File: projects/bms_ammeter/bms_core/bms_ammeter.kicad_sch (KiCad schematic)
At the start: 9 parts, among them IC1 ADS1246IPWR, U2 AP7370-12FDC, U3 ADUM4150ARIZ-RL

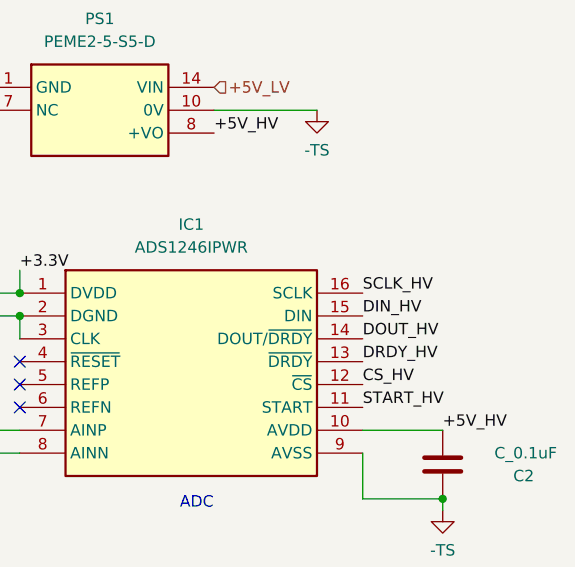
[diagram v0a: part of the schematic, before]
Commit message: Added ammeter to BMS core schematic
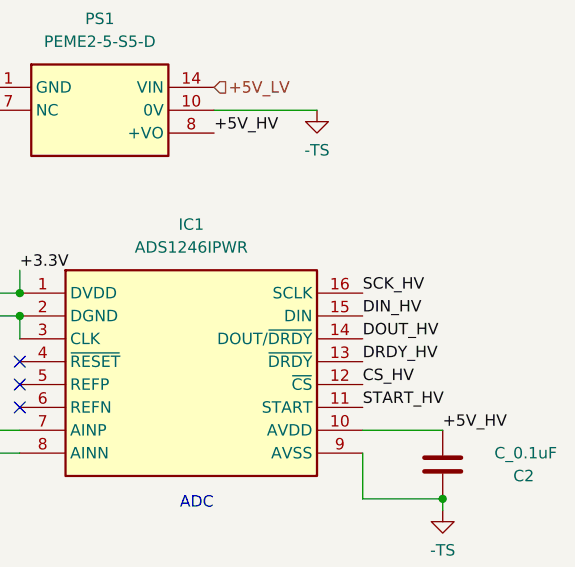
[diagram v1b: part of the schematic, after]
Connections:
- net SCLK_HV is gone; now on net SCK_HV: IC1.16 (SCLK)
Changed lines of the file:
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@@
     (effects (font (size 1.27 1.27)) (justify left bottom))
   )
-  (label "SCLK_HV" (at 191.77 83.82 0) (fields_autoplaced)
+  (label "SCK_HV" (at 191.77 83.82 0) (fields_autoplaced)
     (effects (font (size 1.27 1.27)) (justify left bottom))
   )
@@
     (instances
       (project "bms_core"
-        (path "/19b2a9f9-0be6-4bde-80c5-cbc5126d55d5/fa7f3556-5e5e-451a-bb56-11a595d3a0ce"
+        (path "/19b2a9f9-0be6-4bde-80c5-cbc5126d55d5/ed6af89d-de77-4c92-a6f5-d304e6bc128b"
           (reference "#PWR08") (unit 1)
         )
@@
     (instances
       (project "bms_core"
-        (path "/19b2a9f9-0be6-4bde-80c5-cbc5126d55d5/fa7f3556-5e5e-451a-bb56-11a595d3a0ce"
+        (path "/19b2a9f9-0be6-4bde-80c5-cbc5126d55d5/ed6af89d-de77-4c92-a6f5-d304e6bc128b"
           (reference "#PWR02") (unit 1)
         )
@@
     (instances
       (project "bms_core"
-        (path "/19b2a9f9-0be6-4bde-80c5-cbc5126d55d5/fa7f3556-5e5e-451a-bb56-11a595d3a0ce"
+        (path "/19b2a9f9-0be6-4bde-80c5-cbc5126d55d5/ed6af89d-de77-4c92-a6f5-d304e6bc128b"
           (reference "IC1") (unit 1)
         )
@@
     (instances
       (project "bms_core"
-        (path "/19b2a9f9-0be6-4bde-80c5-cbc5126d55d5/fa7f3556-5e5e-451a-bb56-11a595d3a0ce"
+        (path "/19b2a9f9-0be6-4bde-80c5-cbc5126d55d5/ed6af89d-de77-4c92-a6f5-d304e6bc128b"
           (reference "#PWR01") (unit 1)
         )
@@
     (instances
       (project "bms_core"
-        (path "/19b2a9f9-0be6-4bde-80c5-cbc5126d55d5/fa7f3556-5e5e-451a-bb56-11a595d3a0ce"
+        (path "/19b2a9f9-0be6-4bde-80c5-cbc5126d55d5/ed6af89d-de77-4c92-a6f5-d304e6bc128b"
           (reference "#PWR010") (unit 1)
         )
@@
     (instances
       (project "bms_core"
-        (path "/19b2a9f9-0be6-4bde-80c5-cbc5126d55d5/fa7f3556-5e5e-451a-bb56-11a595d3a0ce"
+        (path "/19b2a9f9-0be6-4bde-80c5-cbc5126d55d5/ed6af89d-de77-4c92-a6f5-d304e6bc128b"
           (reference "U3") (unit 1)
         )
@@
     (instances
       (project "bms_core"
-        (path "/19b2a9f9-0be6-4bde-80c5-cbc5126d55d5/fa7f3556-5e5e-451a-bb56-11a595d3a0ce"
+        (path "/19b2a9f9-0be6-4bde-80c5-cbc5126d55d5/ed6af89d-de77-4c92-a6f5-d304e6bc128b"
           (reference "R1") (unit 1)
         )
@@
     (instances
       (project "bms_core"
-        (path "/19b2a9f9-0be6-4bde-80c5-cbc5126d55d5/fa7f3556-5e5e-451a-bb56-11a595d3a0ce"
+        (path "/19b2a9f9-0be6-4bde-80c5-cbc5126d55d5/ed6af89d-de77-4c92-a6f5-d304e6bc128b"
           (reference "C1") (unit 1)
         )
@@
     (instances
       (project "bms_core"
-        (path "/19b2a9f9-0be6-4bde-80c5-cbc5126d55d5/fa7f3556-5e5e-451a-bb56-11a595d3a0ce"
+        (path "/19b2a9f9-0be6-4bde-80c5-cbc5126d55d5/ed6af89d-de77-4c92-a6f5-d304e6bc128b"
           (reference "PS1") (unit 1)
         )
@@
     (instances
       (project "bms_core"
-        (path "/19b2a9f9-0be6-4bde-80c5-cbc5126d55d5/fa7f3556-5e5e-451a-bb56-11a595d3a0ce"
+        (path "/19b2a9f9-0be6-4bde-80c5-cbc5126d55d5/ed6af89d-de77-4c92-a6f5-d304e6bc128b"
           (reference "#PWR07") (unit 1)
         )
@@
     (instances
       (project "bms_core"
-        (path "/19b2a9f9-0be6-4bde-80c5-cbc5126d55d5/fa7f3556-5e5e-451a-bb56-11a595d3a0ce"
+        (path "/19b2a9f9-0be6-4bde-80c5-cbc5126d55d5/ed6af89d-de77-4c92-a6f5-d304e6bc128b"
           (reference "#PWR03") (unit 1)
         )
@@
     (instances
       (project "bms_core"
-        (path "/19b2a9f9-0be6-4bde-80c5-cbc5126d55d5/fa7f3556-5e5e-451a-bb56-11a595d3a0ce"
+        (path "/19b2a9f9-0be6-4bde-80c5-cbc5126d55d5/ed6af89d-de77-4c92-a6f5-d304e6bc128b"
           (reference "C4") (unit 1)
         )
@@
     (instances
       (project "bms_core"
-        (path "/19b2a9f9-0be6-4bde-80c5-cbc5126d55d5/fa7f3556-5e5e-451a-bb56-11a595d3a0ce"
+        (path "/19b2a9f9-0be6-4bde-80c5-cbc5126d55d5/ed6af89d-de77-4c92-a6f5-d304e6bc128b"
           (reference "C3") (unit 1)
         )
@@
     (instances
       (project "bms_core"
-        (path "/19b2a9f9-0be6-4bde-80c5-cbc5126d55d5/fa7f3556-5e5e-451a-bb56-11a595d3a0ce"
+        (path "/19b2a9f9-0be6-4bde-80c5-cbc5126d55d5/ed6af89d-de77-4c92-a6f5-d304e6bc128b"
           (reference "#PWR09") (unit 1)
         )
@@
     (instances
       (project "bms_core"
-        (path "/19b2a9f9-0be6-4bde-80c5-cbc5126d55d5/fa7f3556-5e5e-451a-bb56-11a595d3a0ce"
+        (path "/19b2a9f9-0be6-4bde-80c5-cbc5126d55d5/ed6af89d-de77-4c92-a6f5-d304e6bc128b"
           (reference "#PWR05") (unit 1)
         )
@@
     (instances
       (project "bms_core"
-        (path "/19b2a9f9-0be6-4bde-80c5-cbc5126d55d5/fa7f3556-5e5e-451a-bb56-11a595d3a0ce"
+        (path "/19b2a9f9-0be6-4bde-80c5-cbc5126d55d5/ed6af89d-de77-4c92-a6f5-d304e6bc128b"
           (reference "#PWR06") (unit 1)
         )
@@
     (instances
       (project "bms_core"
-        (path "/19b2a9f9-0be6-4bde-80c5-cbc5126d55d5/fa7f3556-5e5e-451a-bb56-11a595d3a0ce"
+        (path "/19b2a9f9-0be6-4bde-80c5-cbc5126d55d5/ed6af89d-de77-4c92-a6f5-d304e6bc128b"
           (reference "C2") (unit 1)
         )
@@
     (instances
       (project "bms_core"
-        (path "/19b2a9f9-0be6-4bde-80c5-cbc5126d55d5/fa7f3556-5e5e-451a-bb56-11a595d3a0ce"
+        (path "/19b2a9f9-0be6-4bde-80c5-cbc5126d55d5/ed6af89d-de77-4c92-a6f5-d304e6bc128b"
           (reference "#PWR04") (unit 1)
         )
@@
     (instances
       (project "bms_core"
-        (path "/19b2a9f9-0be6-4bde-80c5-cbc5126d55d5/fa7f3556-5e5e-451a-bb56-11a595d3a0ce"
+        (path "/19b2a9f9-0be6-4bde-80c5-cbc5126d55d5/ed6af89d-de77-4c92-a6f5-d304e6bc128b"
           (reference "U2") (unit 1)
         )

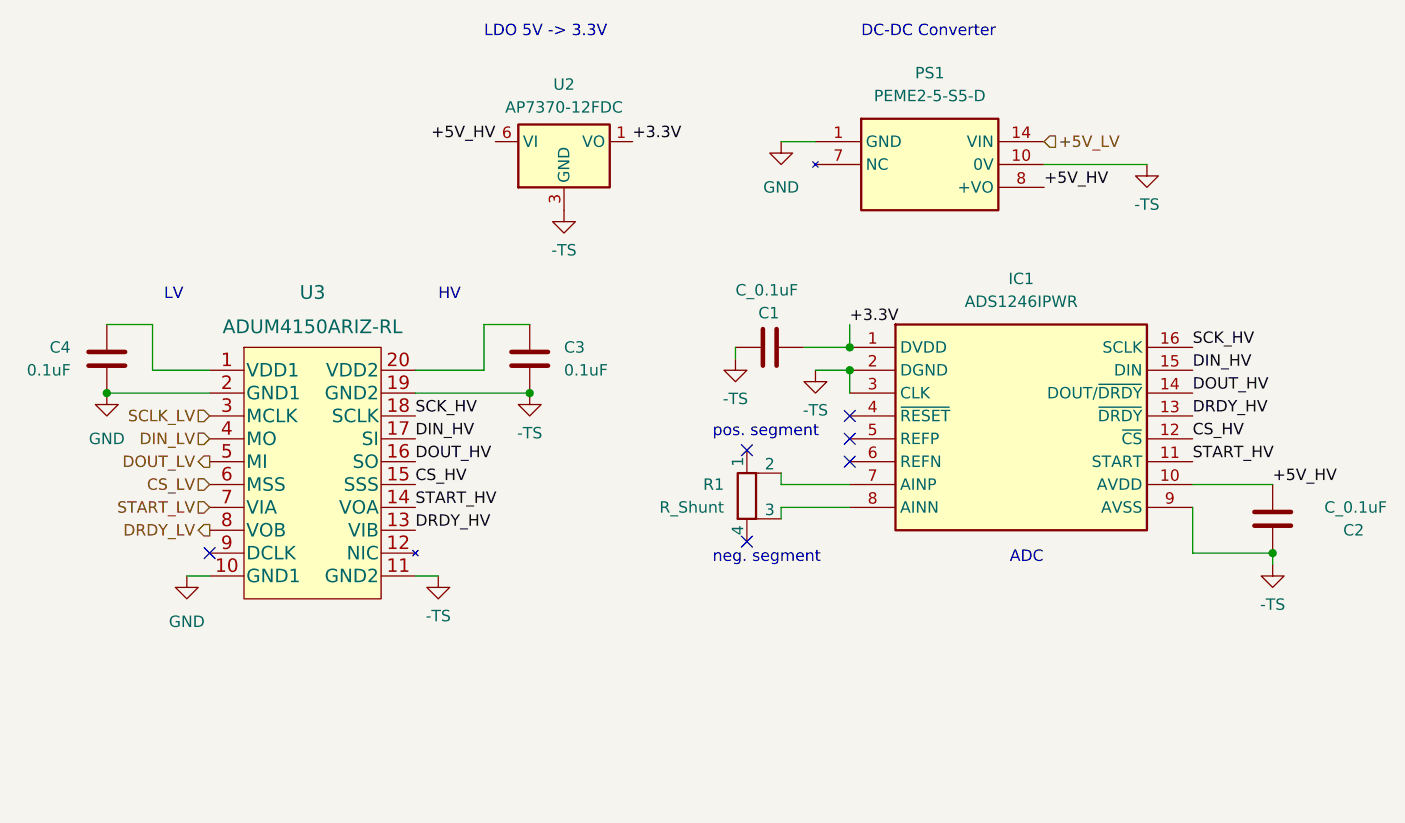
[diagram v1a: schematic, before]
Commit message: Added revisions from Melissa's comments
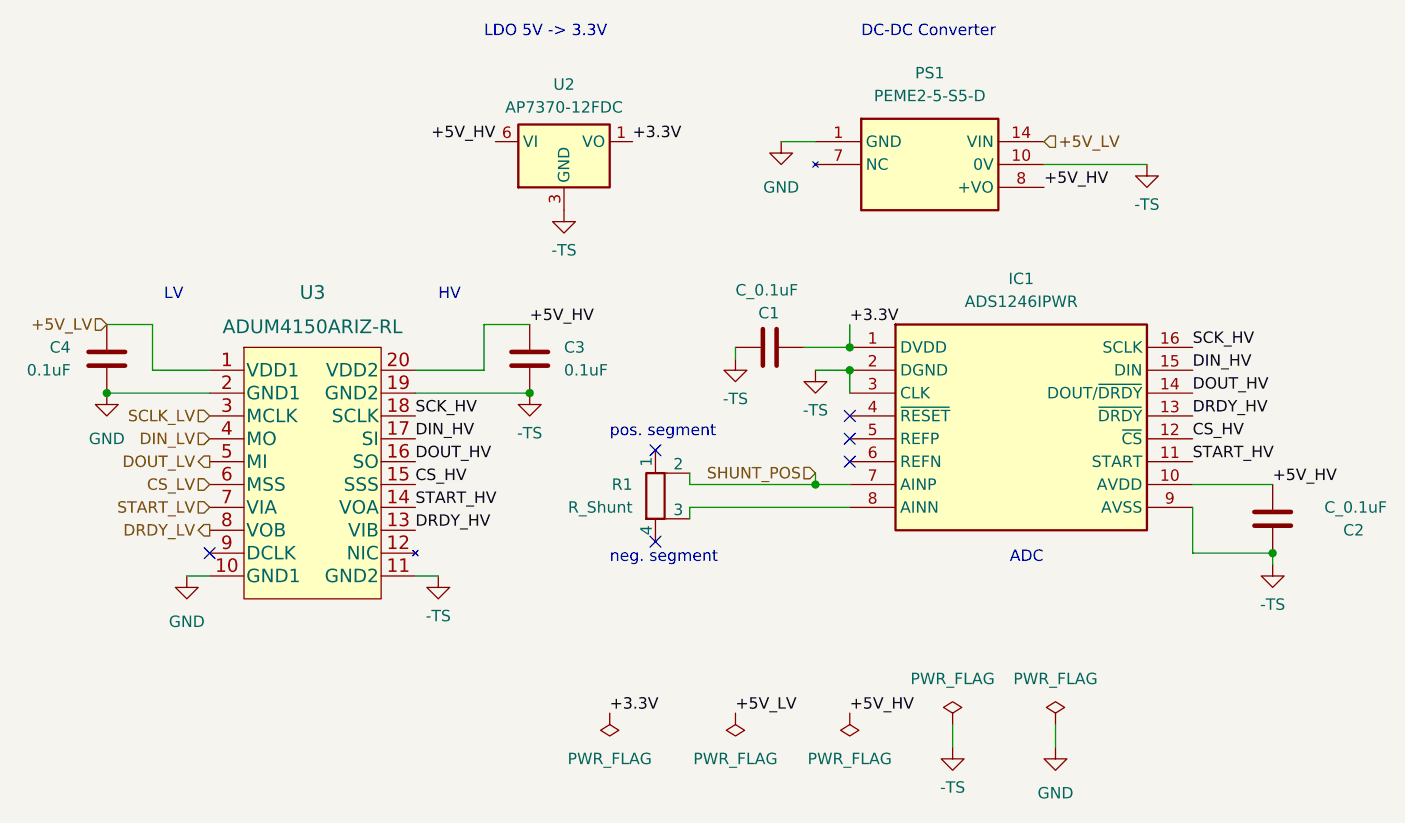
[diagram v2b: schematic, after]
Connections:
- net +5V_HV: now also C3.1, U3.20 (VDD2)
- net +5V_LV: now also C4.1, U3.1 (VDD1)
- net SHUNT_POS: now reaches IC1.7 (AINP), R1.2
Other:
- moved on the sheet: R1
